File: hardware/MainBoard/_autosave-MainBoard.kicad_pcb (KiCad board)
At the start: 4 copper layers, 28.6 x 59.4 mm, 54 parts, among them J1 Conn_02x16_Top_Bottom, J2 Conn_02x16_Top_Bottom, J3 USB_C_Receptacle_USB2.0_16P, J4 En_A, J5 En_B, J6 Micro_SD_Card_Det2, J7 Conn_02x16_Top_Bottom, Q1 MMBT2222A, U1 ESP32-S3-WROOM-1, U2 AMS1117-3.3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

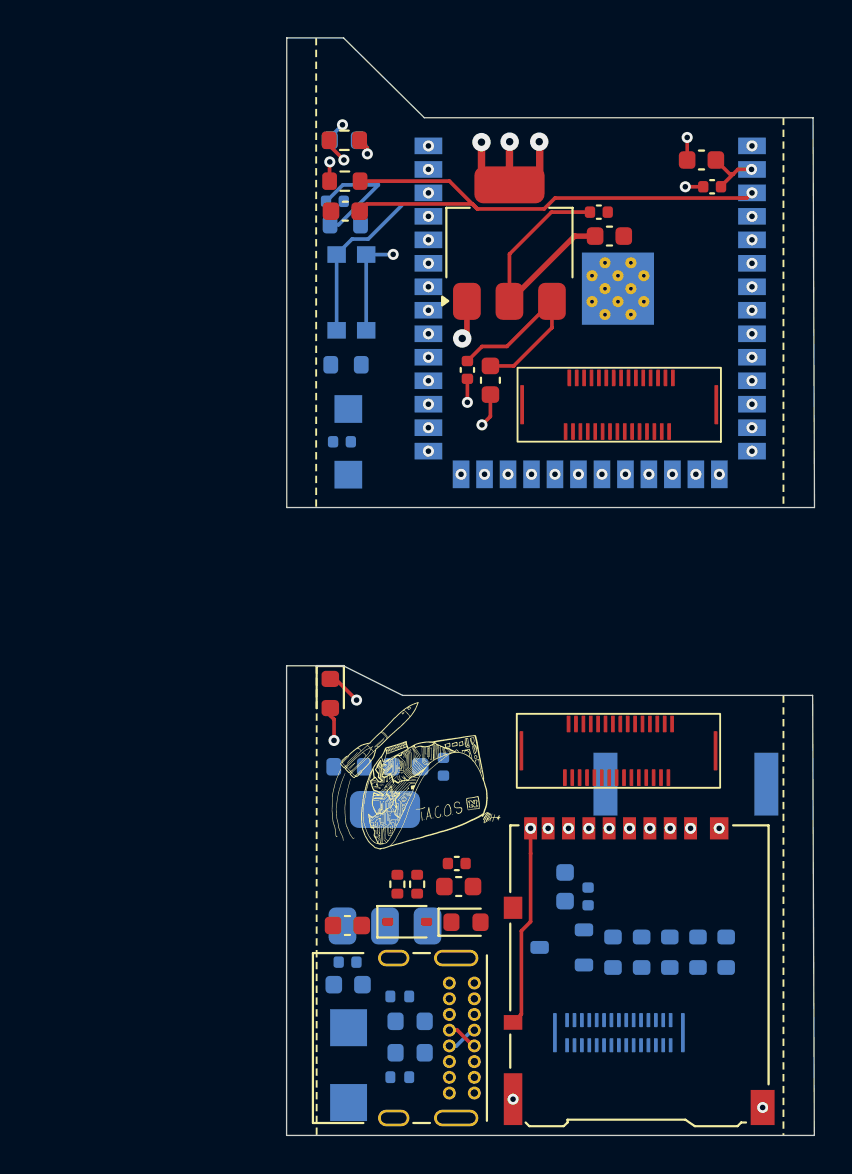
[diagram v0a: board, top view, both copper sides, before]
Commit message: Revert "merge? i might have messed it up"
This reverts commit 9783b900dc87fa86d5773213ec3461e06766d3d4, reversing
changes made to c60a9f34725409086c7bd1e4ee39c0fff9320fd7.
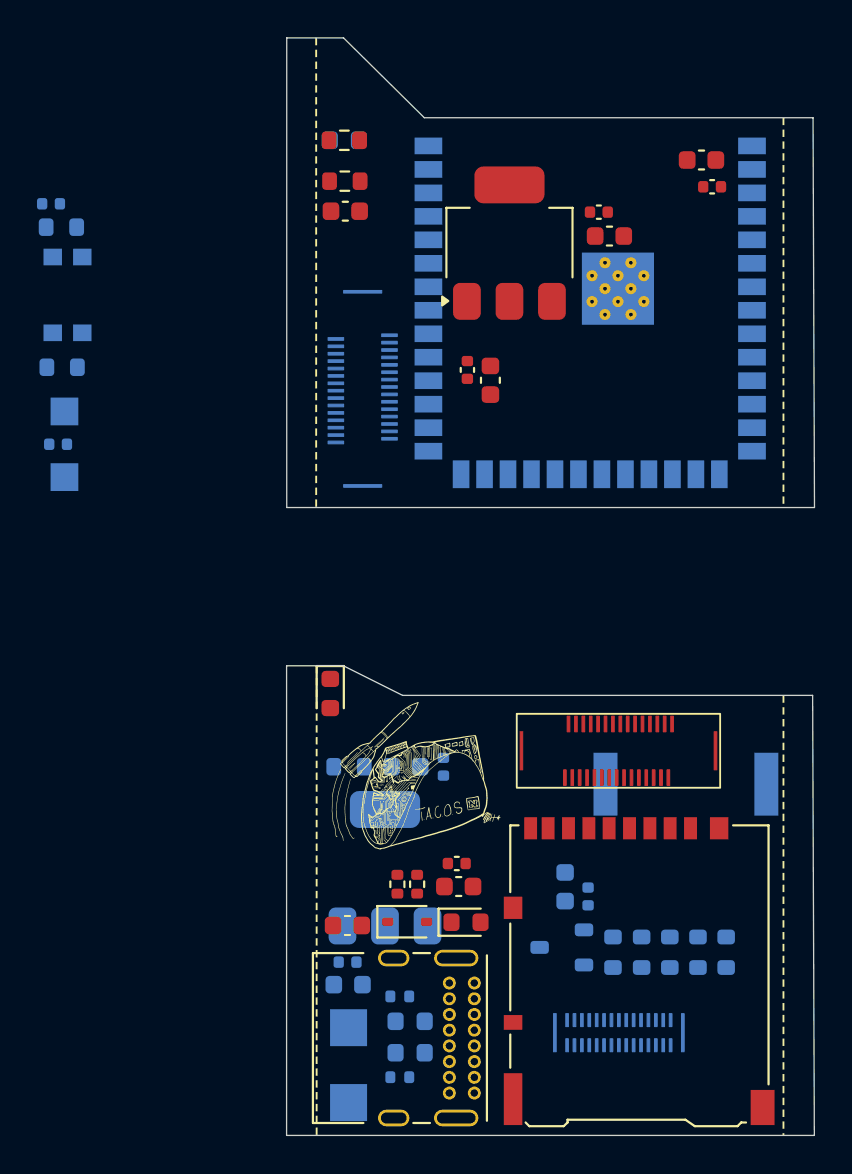
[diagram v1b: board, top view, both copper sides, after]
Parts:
- J2: moved to B.Cu
- moved BOOT1 15.4 mm to (50.5, 64.7)
- moved R12 15.4 mm to (50.2, 68.6)
- moved J4 15.4 mm to (50.3, 71.0)
- moved J5 15.4 mm to (50.3, 74.6)
- moved R10 15.4 mm to (50.1, 61.0)
- moved C14 15.4 mm to (49.6, 59.8)
- moved C16 15.4 mm to (49.9, 72.8)
- moved J2 13.9 mm to (66.4, 69.8), turned to 90 degrees
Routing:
- net CONN_VCC: track 28.9 -> 0.00 mm, vias 7 -> 0
- net CHIP_PU: track 28.8 -> 0.00 mm, vias 1 -> 0
- net CONN_GND: track 16.0 -> 0.00 mm, vias 14 -> 0
- net GPIO0: track 15.4 -> 0.00 mm, vias 1 -> 0
- net CONN_3V: track 11.5 -> 0.00 mm
- net SD_DET: track 10.9 -> 0.00 mm, vias 2 -> 0
- net Net-(D2-A): track 1.98 -> 0.00 mm, vias 1 -> 0
- net Net-(D1-A): track 1.97 -> 0.00 mm, vias 1 -> 0
- net CONN_15: track 1.70 -> 0.00 mm, vias 1 -> 0
- net CONN_14: track 1.70 -> 0.00 mm, vias 1 -> 0
- net CONN_3: track 0.61 -> 0.00 mm, vias 1 -> 0
- net unconnected-(U1-TXD0-Pad37): vias 1 -> 0
- net unconnected-(U1-RXD0-Pad36): vias 1 -> 0
- net unconnected-(U1-IO9-Pad17): vias 1 -> 0
- net unconnected-(U1-IO8-Pad12): vias 1 -> 0
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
